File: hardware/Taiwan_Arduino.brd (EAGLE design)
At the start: 97.2 x 35.7 mm, 44 parts, among them J1 AVR_SPI_PRG_62X3_LOCK, T1 2SC, T2 2N, U1 ATMEGA328P_PDIP, Y2 16mhz

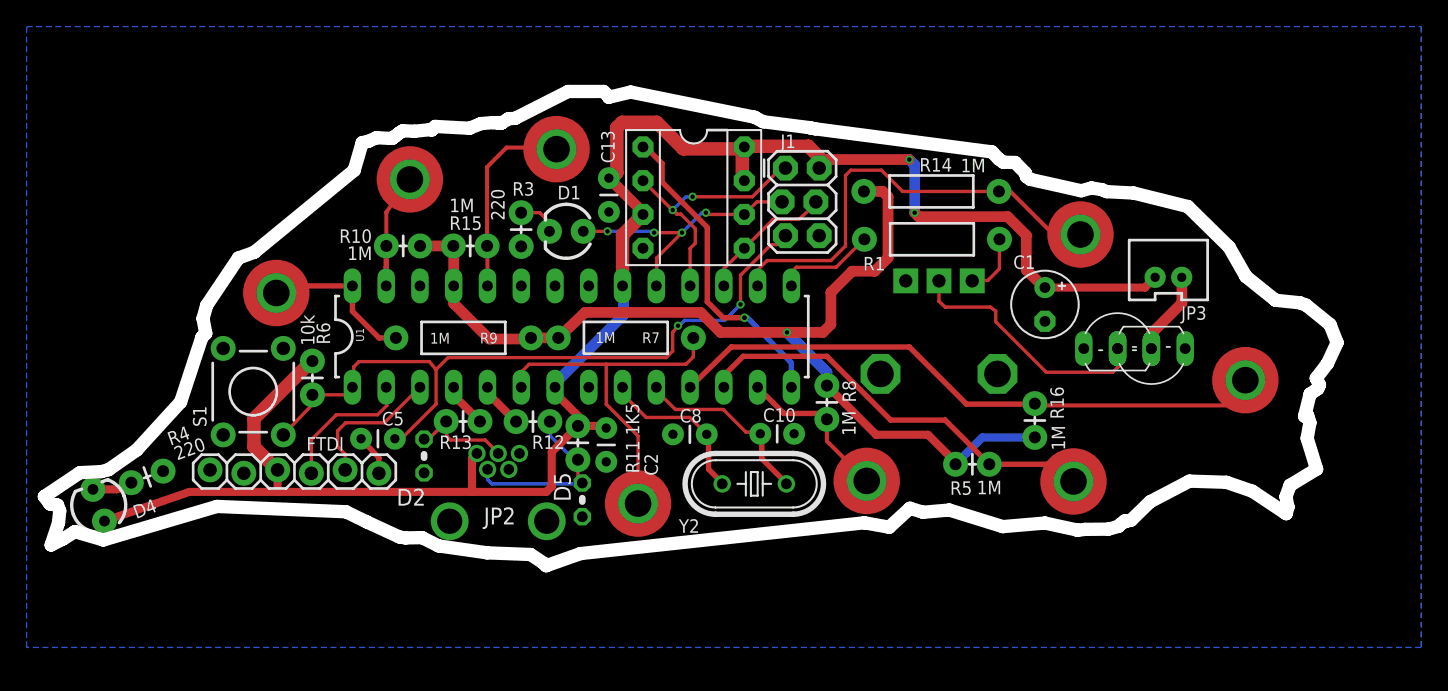
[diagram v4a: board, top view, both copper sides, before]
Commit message: Improve touch pad grounding
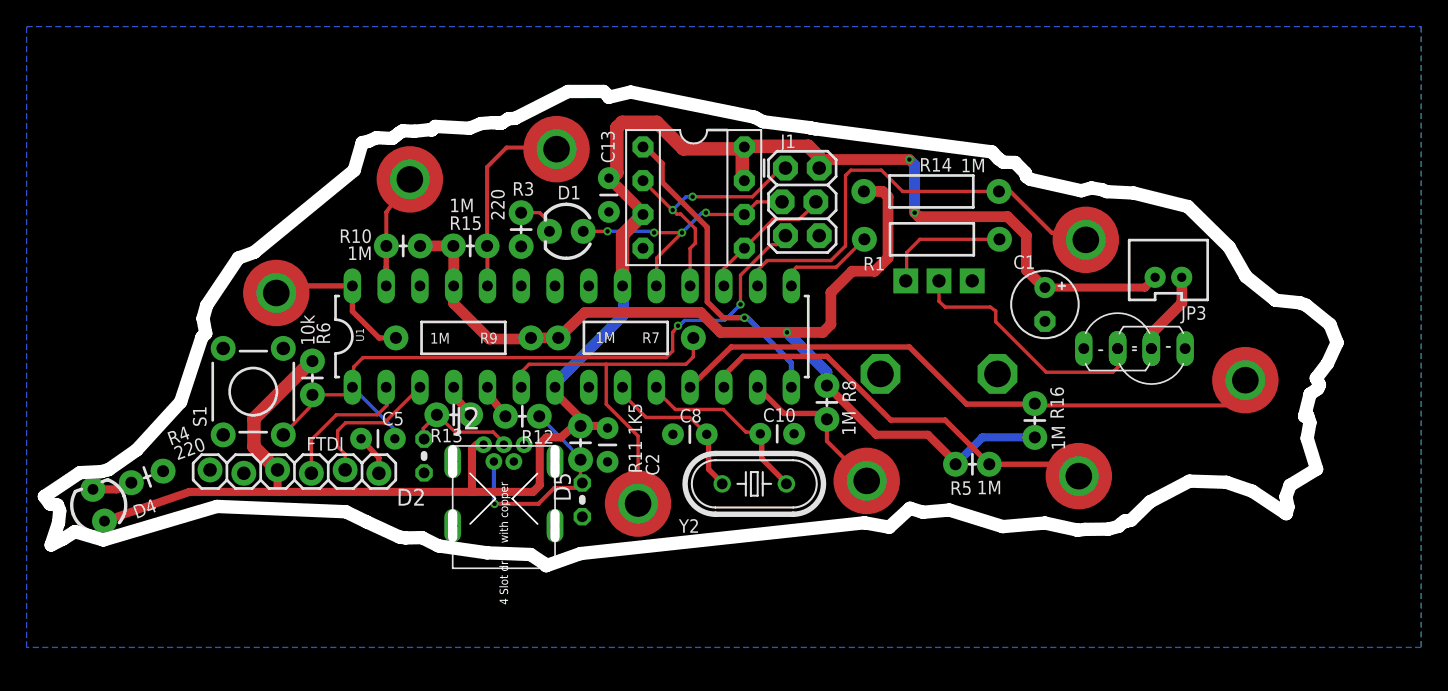
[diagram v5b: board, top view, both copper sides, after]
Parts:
- removed JP2: USB-MB-H, SparkFun-Connectors:USB-MB-H
- added J2: (no value), Connector :MINI-5P
- moved R12 0.89 mm to (36.3, 14.7)
- moved R13 0.86 mm to (33.7, 14.8)
- moved TP9 0.57 mm to (80.0, 28.0)
- moved TP3 0.57 mm to (79.4, 10.2)
- moved R11 0.20 mm to (42.0, 11.4)
- moved C2 0.10 mm to (44.0, 13.8)
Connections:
- net +5V: now also J2.VCC; no longer JP2.VBUS
- net GND: now also J2.GND, J2.S1, J2.S2, J2.S3, J2.S4, RV1.P$1; no longer JP2.GND, RV1.P$3
- net N$1: now also RV1.P$3; no longer RV1.P$1
- net N$15: now also J2.DM; no longer JP2.D-
- net N$16: now also J2.DP; no longer JP2.D+
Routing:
- net N$1: track 4.65 -> 9.55 mm
- net N$15: track 13.9 -> 17.1 mm, vias 0 -> 1
- net RST: track 55.6 -> 53.5 mm
- net +5V: track 138.9 -> 140.1 mm
- net D+: track 3.39 -> 2.55 mm
- net D-: track 3.48 -> 2.65 mm
